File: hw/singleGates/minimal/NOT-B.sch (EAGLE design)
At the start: 3 parts, among them Q1 BC817

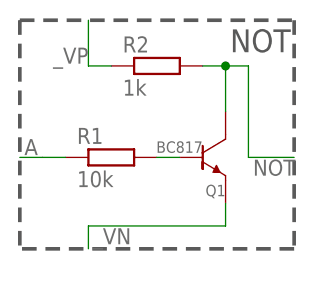
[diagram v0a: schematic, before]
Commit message: fixes some offset and juction issues
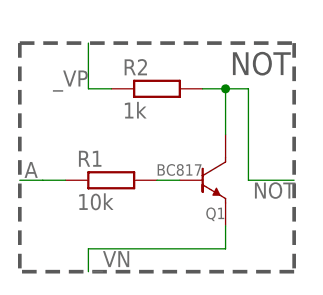
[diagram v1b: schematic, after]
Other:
- moved on the sheet: Q1, R1, R2
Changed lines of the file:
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@@
 <sheet>
 <plain>
-<wire x1="17.78" y1="-10.16" x2="-12.7" y2="-10.16" width="0.4064" layer="97" style="longdash"/>
-<wire x1="-12.7" y1="15.24" x2="-12.7" y2="-10.16" width="0.4064" layer="97" style="longdash"/>
-<wire x1="17.78" y1="15.24" x2="17.78" y2="-10.16" width="0.4064" layer="97" style="longdash"/>
-<wire x1="-12.7" y1="15.24" x2="17.78" y2="15.24" width="0.4064" layer="97" style="longdash"/>
-<text x="10.668" y="11.684" size="2.54" layer="97" ratio="12">NOT</text>
+<wire x1="17.78" y1="-12.7" x2="-12.7" y2="-12.7" width="0.4064" layer="97" style="longdash"/>
+<wire x1="-12.7" y1="12.7" x2="-12.7" y2="-12.7" width="0.4064" layer="97" style="longdash"/>
+<wire x1="17.78" y1="12.7" x2="17.78" y2="-12.7" width="0.4064" layer="97" style="longdash"/>
+<wire x1="-12.7" y1="12.7" x2="17.78" y2="12.7" width="0.4064" layer="97" style="longdash"/>
+<text x="10.668" y="9.144" size="2.54" layer="97" ratio="12">NOT</text>
 </plain>
 <instances>
-<instance part="R1" gate="G$1" x="-2.54" y="0"/>
-<instance part="R2" gate="G$1" x="2.54" y="10.16"/>
-<instance part="Q1" gate="G$1" x="10.16" y="0" smashed="yes">
-<attribute name="NAME" x="10.16" y="-4.318" size="1.27" layer="95" ratio="12" rot="R180" align="top-left"/>
-<attribute name="VALUE" x="7.62" y="1.778" size="1.27" layer="96" ratio="12" rot="R180"/>
+<instance part="R1" gate="G$1" x="-2.54" y="-2.54"/>
+<instance part="R2" gate="G$1" x="2.54" y="7.62"/>
+<instance part="Q1" gate="G$1" x="10.16" y="-2.54" smashed="yes">
+<attribute name="NAME" x="10.16" y="-6.858" size="1.27" layer="95" ratio="12" rot="R180" align="top-left"/>
+<attribute name="VALUE" x="7.62" y="-0.762" size="1.27" layer="96" ratio="12" rot="R180"/>
 </instance>
 </instances>
@@
 <net name="_VN" class="0">
 <segment>
-<wire x1="-5.08" y1="-7.62" x2="10.16" y2="-7.62" width="0.1524" layer="91"/>
-<wire x1="10.16" y1="-7.62" x2="10.16" y2="-5.08" width="0.1524" layer="91"/>
-<label x="-4.572" y="-9.652" size="1.778" layer="95"/>
-<wire x1="-5.08" y1="-7.62" x2="-5.08" y2="-10.16" width="0.1524" layer="91"/>
+<wire x1="-5.08" y1="-10.16" x2="10.16" y2="-10.16" width="0.1524" layer="91"/>
+<wire x1="10.16" y1="-10.16" x2="10.16" y2="-7.62" width="0.1524" layer="91"/>
+<label x="-4.572" y="-12.192" size="1.778" layer="95"/>
+<wire x1="-5.08" y1="-10.16" x2="-5.08" y2="-12.7" width="0.1524" layer="91"/>
 <pinref part="Q1" gate="G$1" pin="EMITTER"/>
 </segment>
@@
 <segment>
 <pinref part="R1" gate="G$1" pin="2"/>
-<wire x1="2.54" y1="0" x2="5.08" y2="0" width="0.1524" layer="91"/>
+<wire x1="2.54" y1="-2.54" x2="5.08" y2="-2.54" width="0.1524" layer="91"/>
 <pinref part="Q1" gate="G$1" pin="BASE"/>
 </segment>
@@
 <net name="NOT" class="0">
 <segment>
-<wire x1="10.16" y1="5.08" x2="10.16" y2="10.16" width="0.1524" layer="91"/>
-<wire x1="10.16" y1="10.16" x2="12.7" y2="10.16" width="0.1524" layer="91"/>
-<wire x1="12.7" y1="10.16" x2="12.7" y2="0" width="0.1524" layer="91"/>
-<wire x1="12.7" y1="0" x2="17.78" y2="0" width="0.1524" layer="91"/>
-<label x="13.208" y="-2.032" size="1.778" layer="95"/>
+<wire x1="10.16" y1="2.54" x2="10.16" y2="7.62" width="0.1524" layer="91"/>
+<wire x1="10.16" y1="7.62" x2="12.7" y2="7.62" width="0.1524" layer="91"/>
+<wire x1="12.7" y1="7.62" x2="12.7" y2="-2.54" width="0.1524" layer="91"/>
+<wire x1="12.7" y1="-2.54" x2="17.78" y2="-2.54" width="0.1524" layer="91"/>
+<label x="13.208" y="-4.572" size="1.778" layer="95"/>
 <pinref part="R2" gate="G$1" pin="2"/>
-<wire x1="10.16" y1="10.16" x2="7.62" y2="10.16" width="0.1524" layer="91"/>
-<junction x="10.16" y="10.16"/>
+<wire x1="10.16" y1="7.62" x2="7.62" y2="7.62" width="0.1524" layer="91"/>
+<junction x="10.16" y="7.62"/>
 <pinref part="Q1" gate="G$1" pin="COLLECTOR"/>
 </segment>
@@
 <segment>
 <pinref part="R1" gate="G$1" pin="1"/>
-<wire x1="-7.62" y1="0" x2="-10.16" y2="0" width="0.1524" layer="91"/>
-<wire x1="-10.16" y1="0" x2="-12.7" y2="0" width="0.1524" layer="91"/>
-<label x="-12.192" y="0.254" size="1.778" layer="95"/>
+<wire x1="-7.62" y1="-2.54" x2="-10.16" y2="-2.54" width="0.1524" layer="91"/>
+<wire x1="-10.16" y1="-2.54" x2="-12.7" y2="-2.54" width="0.1524" layer="91"/>
+<label x="-12.192" y="-2.286" size="1.778" layer="95"/>
 </segment>
 </net>
@@
 <segment>
 <pinref part="R2" gate="G$1" pin="1"/>
-<wire x1="-2.54" y1="10.16" x2="-5.08" y2="10.16" width="0.1524" layer="91"/>
-<wire x1="-5.08" y1="10.16" x2="-5.08" y2="15.24" width="0.1524" layer="91"/>
-<label x="-5.08" y="12.192" size="1.778" layer="95" rot="R180"/>
+<wire x1="-2.54" y1="7.62" x2="-5.08" y2="7.62" width="0.1524" layer="91"/>
+<wire x1="-5.08" y1="7.62" x2="-5.08" y2="12.7" width="0.1524" layer="91"/>
+<label x="-5.08" y="9.652" size="1.778" layer="95" rot="R180"/>
 </segment>
 </net>

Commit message: fixes alignment issues
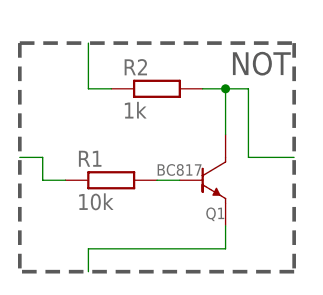
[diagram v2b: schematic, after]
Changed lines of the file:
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@@
 <wire x1="-5.08" y1="-10.16" x2="10.16" y2="-10.16" width="0.1524" layer="91"/>
 <wire x1="10.16" y1="-10.16" x2="10.16" y2="-7.62" width="0.1524" layer="91"/>
-<label x="-4.572" y="-12.192" size="1.778" layer="95"/>
 <wire x1="-5.08" y1="-10.16" x2="-5.08" y2="-12.7" width="0.1524" layer="91"/>
 <pinref part="Q1" gate="G$1" pin="EMITTER"/>
@@
 <wire x1="10.16" y1="2.54" x2="10.16" y2="7.62" width="0.1524" layer="91"/>
 <wire x1="10.16" y1="7.62" x2="12.7" y2="7.62" width="0.1524" layer="91"/>
-<wire x1="12.7" y1="7.62" x2="12.7" y2="-2.54" width="0.1524" layer="91"/>
-<wire x1="12.7" y1="-2.54" x2="17.78" y2="-2.54" width="0.1524" layer="91"/>
-<label x="13.208" y="-4.572" size="1.778" layer="95"/>
+<wire x1="12.7" y1="7.62" x2="12.7" y2="0" width="0.1524" layer="91"/>
+<wire x1="12.7" y1="0" x2="17.78" y2="0" width="0.1524" layer="91"/>
 <pinref part="R2" gate="G$1" pin="2"/>
 <wire x1="10.16" y1="7.62" x2="7.62" y2="7.62" width="0.1524" layer="91"/>
@@
 <pinref part="R1" gate="G$1" pin="1"/>
 <wire x1="-7.62" y1="-2.54" x2="-10.16" y2="-2.54" width="0.1524" layer="91"/>
-<wire x1="-10.16" y1="-2.54" x2="-12.7" y2="-2.54" width="0.1524" layer="91"/>
-<label x="-12.192" y="-2.286" size="1.778" layer="95"/>
+<wire x1="-10.16" y1="-2.54" x2="-10.16" y2="0" width="0.1524" layer="91"/>
+<wire x1="-10.16" y1="0" x2="-12.7" y2="0" width="0.1524" layer="91"/>
 </segment>
 </net>
@@
 <wire x1="-2.54" y1="7.62" x2="-5.08" y2="7.62" width="0.1524" layer="91"/>
 <wire x1="-5.08" y1="7.62" x2="-5.08" y2="12.7" width="0.1524" layer="91"/>
-<label x="-5.08" y="9.652" size="1.778" layer="95" rot="R180"/>
 </segment>
 </net>

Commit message: Add led output and prepare first alu slice
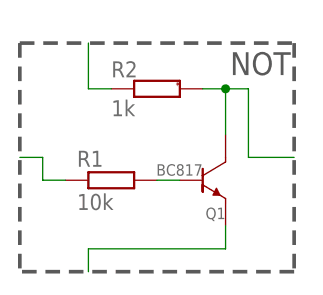
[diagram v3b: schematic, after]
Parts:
- R2: device p.peter-gator:R-EU_R0603 -> p.peter-rcl:R-EU-MARKEDR0603
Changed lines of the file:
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@@
 <parts>
 <part name="R1" library="p.peter-gator" deviceset="R-EU_" device="R0603" value="10k"/>
-<part name="R2" library="p.peter-gator" deviceset="R-EU_" device="R0603" value="1k"/>
+<part name="R2" library="p.peter-rcl" deviceset="R-EU-MARKED" device="R0603" value="1k"/>
 <part name="Q1" library="p.peter-gator" deviceset="TRANSISTOR-NPN-GENERIC" device="-SOT23-BEC" technology="DEFAULT" value="BC817"/>
 </parts>
